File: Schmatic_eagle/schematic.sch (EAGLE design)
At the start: 9 parts, among them IC1 MEGA16-M, IC2 MC145026D, M1 WIRELESS-XY-FST

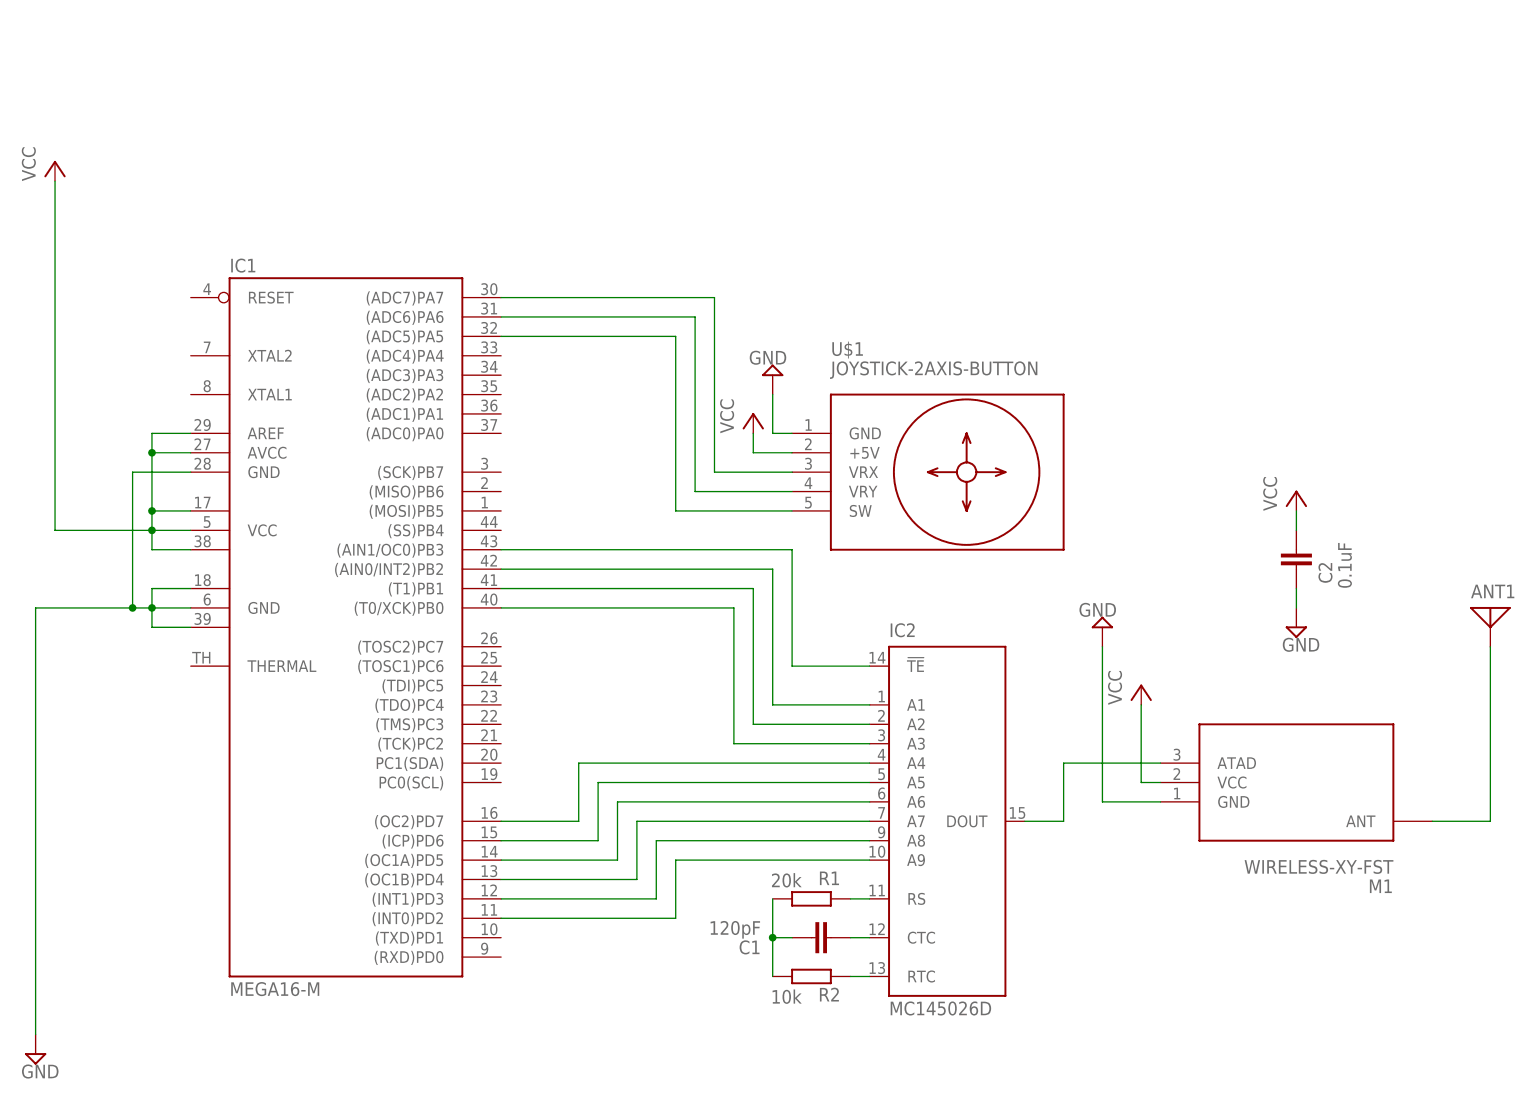
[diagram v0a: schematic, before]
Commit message: Schematic updates
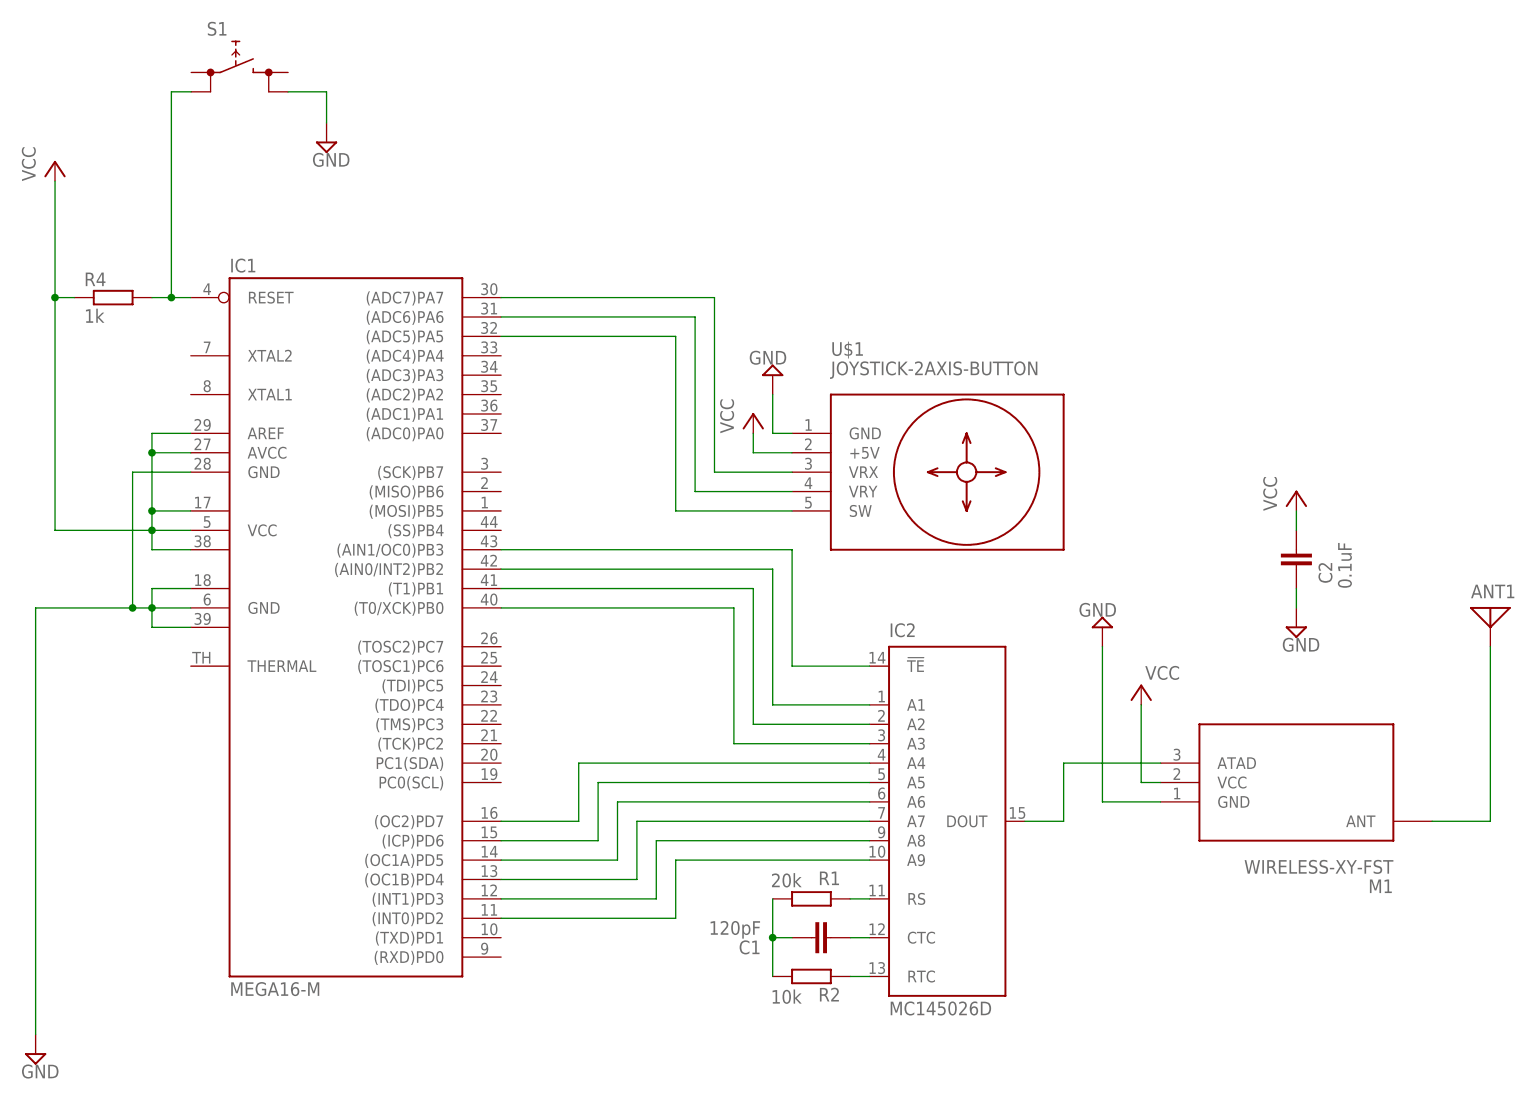
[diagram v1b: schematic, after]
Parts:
- added R4: 1k, rcl:R-EU_01005
- added S1: (no value), switch:REKN
- IC1: SPICEPREFIX (none) -> X
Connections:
- new net N$16: IC1.RESET, R4.2, S1.0@B
- net GND: now also S1.1@B
- net VCC: now also R4.1
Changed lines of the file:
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@@
 </classes>
 <parts>
-<part name="IC1" library="atmel" library_urn="urn:adsk.eagle:library:105" deviceset="MEGA16-M" device="" package3d_urn="urn:adsk.eagle:package:4352/1"/>
+<part name="IC1" library="atmel" library_urn="urn:adsk.eagle:library:105" deviceset="MEGA16-M" device="" package3d_urn="urn:adsk.eagle:package:4352/1">
+<attribute name="SPICEPREFIX" value="X"/>
+</part>
 <part name="U$1" library="diy-modules" deviceset="JOYSTICK-2AXIS-BUTTON" device=""/>
 <part name="SUPPLY2" library="supply2" library_urn="urn:adsk.eagle:library:372" deviceset="GND" device=""/>
@@
 <part name="P+4" library="supply1" library_urn="urn:adsk.eagle:library:371" deviceset="VCC" device=""/>
 <part name="C2" library="capacitor-wima" library_urn="urn:adsk.eagle:library:116" deviceset="C" device="2,5-3" package3d_urn="urn:adsk.eagle:package:5436/1" value="0.1uF"/>
+<part name="S1" library="switch" library_urn="urn:adsk.eagle:library:380" deviceset="REKN" device="" package3d_urn="urn:adsk.eagle:package:27692/1"/>
+<part name="R4" library="rcl" library_urn="urn:adsk.eagle:library:334" deviceset="R-EU_" device="01005" package3d_urn="urn:adsk.eagle:package:26133/2" value="1k"/>
+<part name="SUPPLY5" library="supply2" library_urn="urn:adsk.eagle:library:372" deviceset="GND" device=""/>
 </parts>
 <sheets>
@@
 </instance>
 <instance part="P+3" gate="VCC" x="269.24" y="106.68" smashed="yes">
-<attribute name="VALUE" x="266.7" y="104.14" size="1.778" layer="96" rot="R90"/>
+<attribute name="VALUE" x="274.32" y="109.22" size="1.778" layer="96" rot="R180"/>
 </instance>
 <instance part="SUPPLY3" gate="GND" x="264.16" y="114.3" smashed="yes" rot="R180">
@@
 <attribute name="NAME" x="292.481" y="122.936" size="1.778" layer="95" rot="R270"/>
 <attribute name="VALUE" x="295.021" y="125.476" size="1.778" layer="96" rot="R270"/>
+</instance>
+<instance part="S1" gate="G$1" x="149.911796875" y="186.961290625" smashed="yes">
+<attribute name="NAME" x="146.863796875" y="191.787290625" size="1.778" layer="95"/>
+<attribute name="VALUE" x="146.101796875" y="181.373290625" size="1.778" layer="96"/>
+</instance>
+<instance part="R4" gate="G$1" x="134.62" y="157.48" smashed="yes">
+<attribute name="NAME" x="130.81" y="158.9786" size="1.778" layer="95"/>
+<attribute name="VALUE" x="130.81" y="154.178" size="1.778" layer="96"/>
+</instance>
+<instance part="SUPPLY5" gate="GND" x="162.56" y="177.8" smashed="yes">
+<attribute name="VALUE" x="160.655" y="174.625" size="1.778" layer="96"/>
 </instance>
 </instances>
@@
 <segment>
 <pinref part="P+2" gate="VCC" pin="VCC"/>
-<wire x1="127" y1="172.72" x2="127" y2="127" width="0.1524" layer="91"/>
+<wire x1="127" y1="172.72" x2="127" y2="157.48" width="0.1524" layer="91"/>
 <pinref part="IC1" gate="G$1" pin="VCC"/>
+<wire x1="127" y1="157.48" x2="127" y2="127" width="0.1524" layer="91"/>
 <wire x1="127" y1="127" x2="139.7" y2="127" width="0.1524" layer="91"/>
 <junction x="139.7" y="127"/>
@@
 <wire x1="139.7" y1="139.7" x2="139.7" y2="137.16" width="0.1524" layer="91"/>
 <junction x="139.7" y="137.16"/>
+<pinref part="R4" gate="G$1" pin="1"/>
+<wire x1="129.54" y1="157.48" x2="127" y2="157.48" width="0.1524" layer="91"/>
+<junction x="127" y="157.48"/>
 </segment>
 <segment>
@@
 <wire x1="289.56" y1="116.84" x2="289.56" y2="119.38" width="0.1524" layer="91"/>
 </segment>
+<segment>
+<pinref part="S1" gate="G$1" pin="1@B"/>
+<wire x1="157.531796875" y1="184.421290625" x2="162.56" y2="184.421290625" width="0.1524" layer="91"/>
+<pinref part="SUPPLY5" gate="GND" pin="GND"/>
+<wire x1="162.56" y1="184.421290625" x2="162.56" y2="180.34" width="0.1524" layer="91"/>
+</segment>
 </net>
 <net name="N$4" class="0">
@@
 </segment>
 </net>
+<net name="N$16" class="0">
+<segment>
+<pinref part="S1" gate="G$1" pin="0@B"/>
+<wire x1="144.831796875" y1="184.421290625" x2="142.24" y2="184.421290625" width="0.1524" layer="91"/>
+<wire x1="142.24" y1="184.421290625" x2="142.24" y2="157.48" width="0.1524" layer="91"/>
+<pinref part="IC1" gate="G$1" pin="RESET"/>
+<wire x1="142.24" y1="157.48" x2="144.78" y2="157.48" width="0.1524" layer="91"/>
+<pinref part="R4" gate="G$1" pin="2"/>
+<wire x1="139.7" y1="157.48" x2="142.24" y2="157.48" width="0.1524" layer="91"/>
+<junction x="142.24" y="157.48"/>
+</segment>
+</net>

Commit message: Schematic updtes
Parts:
- added J1: (no value), con-amp:MTA02-100
- added LED1, LED2, LED3: (no value), led:LEDCHIPLED_1206
- added R3: 100, rcl:R-EU_M0805
- R1: device rcl:R-EU_01005 -> rcl:R-EU_M0805
- R2, R4: device rcl:R-EU_01005 -> rcl:R-EU_R0805
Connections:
- new net N$22: IC1.(ADC4)PA4, LED3.A
- new net N$23: IC1.(ADC2)PA2, LED1.A
- new net N$24: IC1.(ADC0)PA0, LED2.A
- new net N$25: LED1.C, LED2.C, LED3.C, R3.1
- net GND: now also J1.2, R3.2
- net VCC: now also J1.1
